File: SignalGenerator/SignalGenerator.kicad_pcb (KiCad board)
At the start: 4 copper layers, 39 parts, among them J1 Buss PD, J2 AVR-ICSP, J3 I2C Display, J4 Conn_Coaxial, J5 Screw_Terminal_01x04, SW1 SW_Push_SPDT, U2 ATmega328P-AU, U5 AD8021, U6 AD9833BRMZ, X1 Oscillator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

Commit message: adf
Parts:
- removed C1: 10uF, Capacitor_SMD:C_1206_3216Metric_Pad1.33x1.80mm_HandSolder
- removed C5: 1uF, Capacitor_SMD:C_0805_2012Metric_Pad1.18x1.45mm_HandSolder
- removed C6: 100nF, Capacitor_SMD:C_0805_2012Metric_Pad1.18x1.45mm_HandSolder
- removed RV1: 1k, Connector_PinHeader_2.54mm:PinHeader_1x03_P2.54mm_Vertical
- removed RV2: 25k, Connector_PinHeader_2.54mm:PinHeader_1x03_P2.54mm_Vertical
- U2: value ATmega328P-AU -> ATmega328-A
- moved C24 102.3 mm to (228.1, 129.8)
- moved C21 94.7 mm to (214.1, 71.4)
- moved C10 83.2 mm to (231.1, 116.6)
- moved C26 61.3 mm to (220.0, 125.5)
- moved C22 60.9 mm to (233.9, 57.4)
- moved R6 58.0 mm to (221.5, 71.4)
- moved R5 54.3 mm to (213.4, 62.5), turned to 90 degrees
- moved C20 52.2 mm to (211.6, 132.3)
- moved C9 50.6 mm to (148.6, 114.3)
- moved C19 49.4 mm to (219.7, 132.1)
- moved R8 45.8 mm to (233.7, 76.2)
- moved C23 43.7 mm to (229.1, 122.2)
- moved U6 43.4 mm to (217.4, 116.6), turned to 0 degrees
- moved U5 40.9 mm to (220.5, 64.0)
- moved C17 40.3 mm to (158.0, 107.7)
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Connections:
- R6 pad 2: Vout -> VOut

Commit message: First real revision to the PCB done.
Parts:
- added G***: LOGO, LOGO, F.Cu at (159.6, 96.7)
- added REF**: MountingHole_3.2mm_M3, MountingHole:MountingHole_3.2mm_M3, F.Cu at (124.0, 114.5)
- added REF**: MountingHole_3.2mm_M3, MountingHole:MountingHole_3.2mm_M3, F.Cu at (124.0, 78.5)
- added REF**: MountingHole_3.2mm_M3, MountingHole:MountingHole_3.2mm_M3, F.Cu at (194.0, 114.5)
- added REF**: MountingHole_3.2mm_M3, MountingHole:MountingHole_3.2mm_M3, F.Cu at (194.0, 78.5)
- added RV1: 1k, Connector_PinHeader_2.54mm:PinHeader_1x03_P2.54mm_Vertical, F.Cu at (184.0, 108.8)
- added RV2: 25k, Connector_PinHeader_2.54mm:PinHeader_1x03_P2.54mm_Vertical, F.Cu at (177.3, 106.8)
- moved C10 95.0 mm to (136.9, 104.8), turned to 180 degrees
- moved C22 90.4 mm to (162.8, 113.2), turned to 90 degrees
- moved R8 85.2 mm to (158.0, 115.3)
- moved R7 84.3 mm to (167.0, 105.4), turned to 90 degrees
- moved J4 76.3 mm to (173.5, 115.6), turned to 90 degrees
- moved C25 71.7 mm to (172.0, 110.0), turned to -90 degrees
- moved U5 71.3 mm to (167.6, 111.8), turned to -90 degrees
- moved R1 66.0 mm to (130.6, 91.1), turned to 90 degrees
- moved J2 63.5 mm to (140.1, 85.2), turned to -90 degrees
- moved C21 63.2 mm to (162.8, 108.3), turned to 90 degrees
- moved SW1 63.0 mm to (181.3, 102.6), turned to 90 degrees
- moved R5 61.5 mm to (170.2, 106.3), turned to 0 degrees
- moved R2 59.8 mm to (124.4, 95.9), turned to -90 degrees
- moved C19 58.7 mm to (178.1, 90.6), turned to -90 degrees
- moved C24 58.6 mm to (179.9, 96.4), turned to -90 degrees
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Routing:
- net GND: track 0.00 -> 106.9 mm, vias 0 -> 49
- net +12V: track 0.00 -> 72.6 mm, vias 0 -> 1
- net -12V: track 0.00 -> 63.8 mm, vias 0 -> 12
- net +5V: track 0.00 -> 61.8 mm, vias 0 -> 19
- net MOSI: track 0.00 -> 52.1 mm, vias 0 -> 2
- net SCLK: track 0.00 -> 47.4 mm, vias 0 -> 2
- net RESET: track 0.00 -> 39.7 mm
- net PD7: track 0.00 -> 37.0 mm
- net PD5: track 0.00 -> 34.1 mm
- net FSYNC: track 0.00 -> 31.4 mm
- net PD6: track 0.00 -> 30.4 mm
- net Net-(J4-Pad1): track 0.00 -> 25.2 mm
- net PD0: track 0.00 -> 19.5 mm
- net Net-(R7-Pad2): track 0.00 -> 18.6 mm
- net PD2: track 0.00 -> 16.6 mm
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- added copper zone on F.Cu, net +5V
- added copper zone on In2.Cu, net +5V
- added copper zone on B.Cu, net -12V
- added copper zone on F.Cu, net -12V
- added copper zone on F.Cu, net GND
- added copper zone on In1.Cu, net GND
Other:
- board outline added: 78 x 44 mm
- board text added: "(C) 2022 Joachim Westlund"
- board text added: "+12V"
- board text added: "+5V"
- board text added: "-12V"
- board text added: "GND"
- board text added: "Signal Generator V0.2"

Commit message: Separeated powersupply to it's own project. Did some stuff to the reset circuit.
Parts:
- removed C13: 10uF, Capacitor_SMD:C_1206_3216Metric_Pad1.33x1.80mm_HandSolder
- removed G***: LOGO, LOGO
- added J6: Power, Connector_PinHeader_2.54mm:PinHeader_2x02_P2.54mm_Vertical, F.Cu at (149.0, 110.6)
- R4: value 10k -> 4.7k
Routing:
- net +12V: track 72.6 -> 101.0 mm
- net -12V: track 63.8 -> 69.5 mm
- net +5V: track 61.8 -> 65.5 mm, vias 19 -> 28
- net GND: track 106.9 -> 108.1 mm, vias 49 -> 54
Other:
- board text added: "1"
- board text added: "2"
- board text added: "3"
- board text added: "Center"
- board text added: "ICP"
- board text added: "LCD I2C"
- board text added: "MISO"
- board text added: "MOSI"
- board text added: "Pin2"
- board text added: "Port D"
- board text added: "RST"
- board text added: "SCLK"
- board text added: "Signal Generator V0.3"
- board text added: "VTG"
- board text removed: "Signal Generator V0.2"

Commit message: new logo
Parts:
- added ?: , LOGO, B.Cu at (157.0, 98.4)

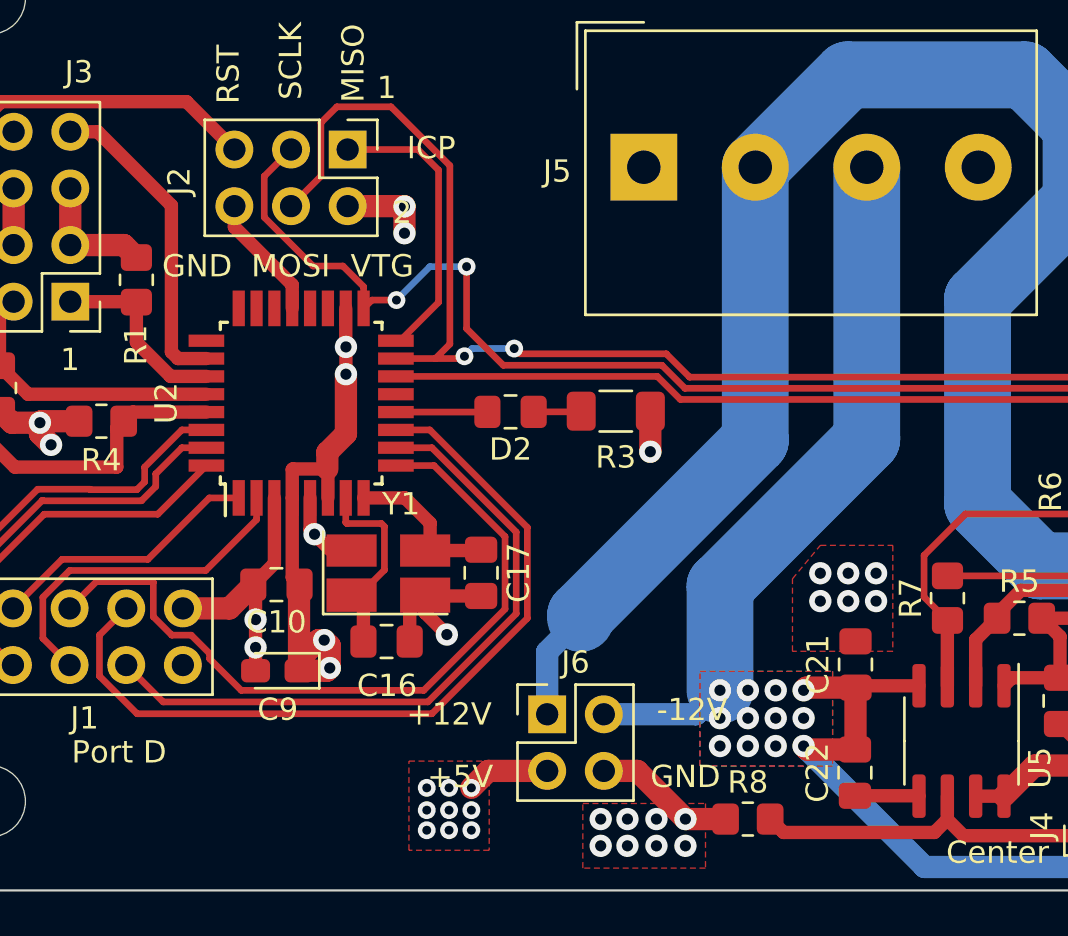
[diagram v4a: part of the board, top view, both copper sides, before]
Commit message: added rotary encoder stuff
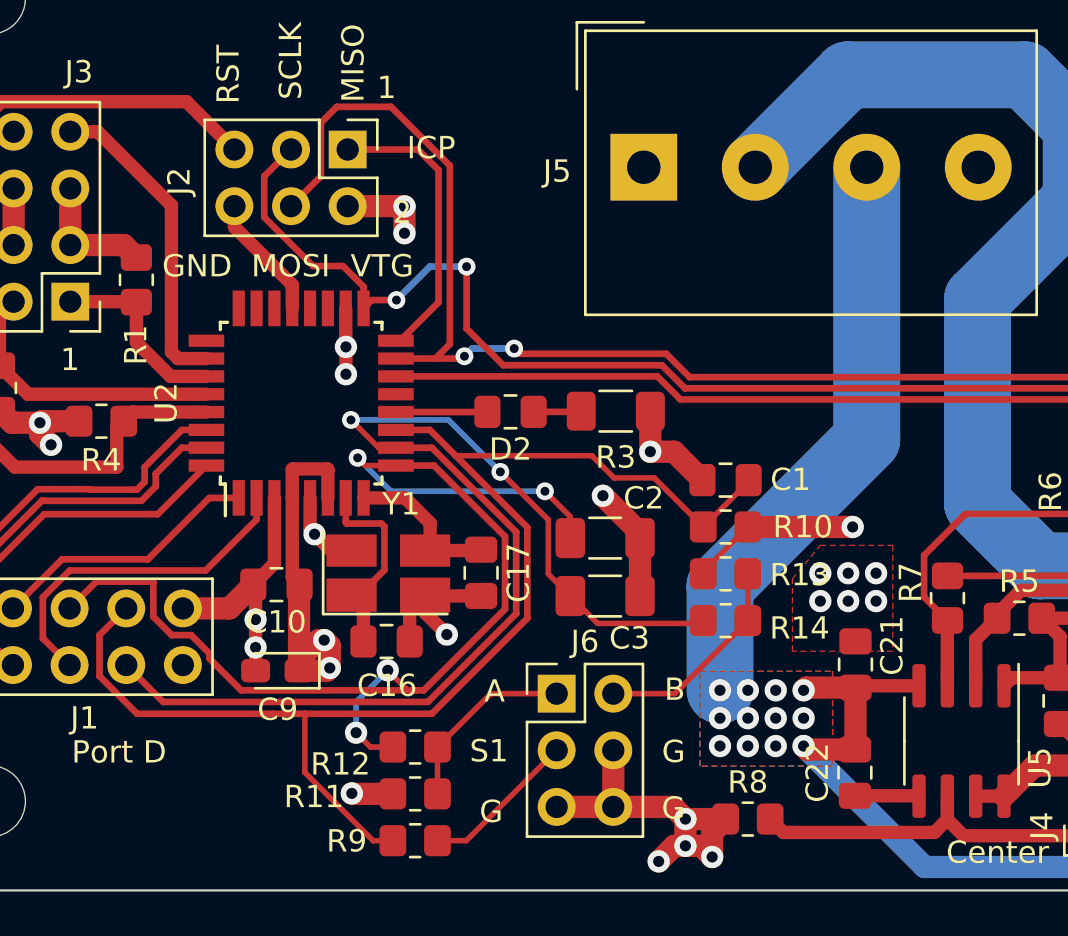
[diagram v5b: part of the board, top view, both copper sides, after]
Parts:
- added C1: 0.1uF, Capacitor_SMD:C_0805_2012Metric_Pad1.18x1.45mm_HandSolder, F.Cu at (157.0, 100.1)
- added C2: 10nF, Capacitor_SMD:C_1206_3216Metric_Pad1.33x1.80mm_HandSolder, F.Cu at (151.6, 102.7)
- added C3: 10nF, Capacitor_SMD:C_1206_3216Metric_Pad1.33x1.80mm_HandSolder, F.Cu at (151.6, 105.3)
- added R10: 10k, Resistor_SMD:R_0805_2012Metric_Pad1.20x1.40mm_HandSolder, F.Cu at (157.0, 102.2)
- added R11: 10k, Resistor_SMD:R_0805_2012Metric_Pad1.20x1.40mm_HandSolder, F.Cu at (143.1, 114.1)
- added R12: 10k, Resistor_SMD:R_0805_2012Metric_Pad1.20x1.40mm_HandSolder, F.Cu at (143.1, 112.0)
- added R13: 10k, Resistor_SMD:R_0805_2012Metric_Pad1.20x1.40mm_HandSolder, F.Cu at (157.0, 104.3)
- added R14: 10k, Resistor_SMD:R_0805_2012Metric_Pad1.20x1.40mm_HandSolder, F.Cu at (157.0, 106.4)
- added R9: 1k, Resistor_SMD:R_0805_2012Metric_Pad1.20x1.40mm_HandSolder, F.Cu at (143.1, 116.2)
- J6: value Power -> RotaryEncoder; footprint Connector_PinHeader_2.54mm:PinHeader_2x02_P2.54mm_Vertical -> Connector_PinHeader_2.54mm:PinHeader_2x03_P2.54mm_Vertical
- moved J6 1.02 mm to (149.4, 109.7)
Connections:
- J6 pad 1: +12V -> A
- J6 pad 2: -12V -> B
- J6 pad 3: +5V -> S1
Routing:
- net +12V: track 101.0 -> 72.6 mm
- net PD6: track 30.4 -> 54.0 mm, vias 0 -> 2
- net PD7: track 37.0 -> 60.2 mm
- net PD5: track 34.1 -> 54.5 mm, vias 0 -> 4
- net GND: track 108.1 -> 126.1 mm, vias 54 -> 51
- net B: track 0.00 -> 9.49 mm
- net A: track 0.00 -> 8.44 mm
- net S1: track 0.00 -> 7.02 mm
- net -12V: track 69.5 -> 63.8 mm
- net +5V: track 65.5 -> 66.6 mm, vias 28 -> 21
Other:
- board text added: "A"
- board text added: "B"
- board text added: "G"
- board text added: "S1"

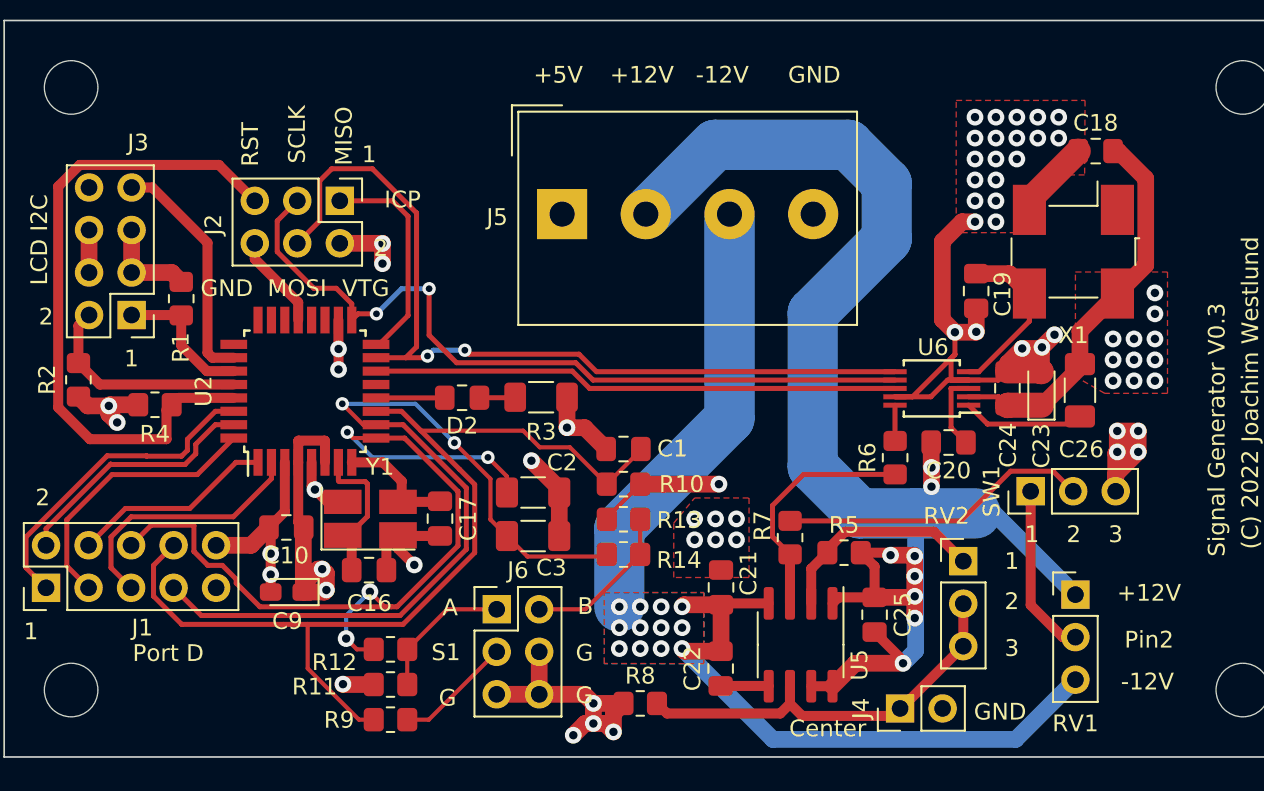
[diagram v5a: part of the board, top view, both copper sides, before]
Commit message: Did alot of changes to my vias. jlcpcb does not support blind or buried vias
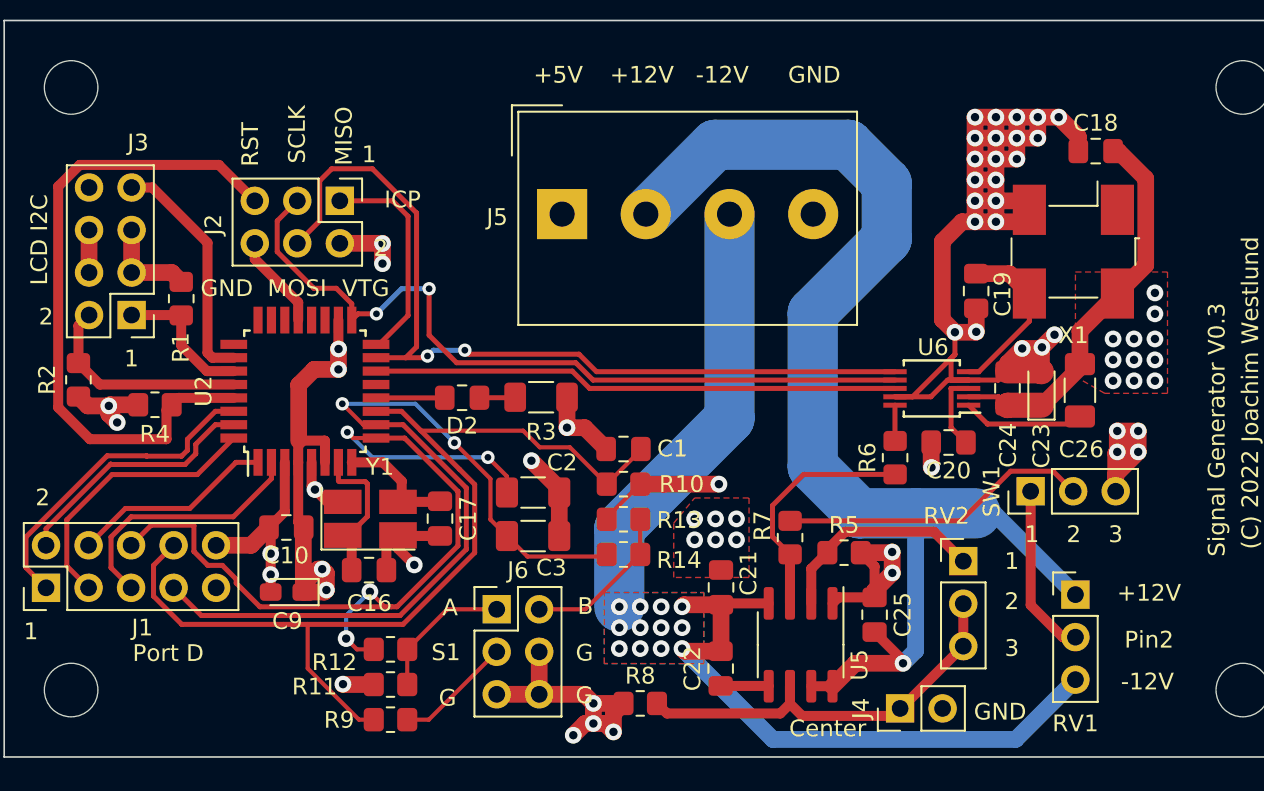
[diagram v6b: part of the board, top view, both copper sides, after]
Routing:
- net GND: track 126.1 -> 154.9 mm, vias 51 -> 46
- net +5V: track 66.6 -> 72.8 mm
